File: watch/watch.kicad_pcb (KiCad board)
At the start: 2 copper layers, 118 parts, among them IC1 MAX77659AENV+, IC2 MAX86141ENP+T, IC3 MAX32664GTGC+T, IC4 TXS0108ERGYR, J1 TYPE-C-31-M-12, J2 Conn_01x02_Socket, J3 Conn_ARM_JTAG_SWD_10, J4 505110-2291, Q1 BSS138, U1 nRF52840, U2 ICM-20602, Y1 FA-128_32.0000MF10Z-AJ5, Y2 CM7V-T1A-32.768kHz-6pF-20PPM-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

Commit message: RTC, board started
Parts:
- removed S5: EVP-ATAL1B000, EVP-ATAL1B000:EVPATAL1B000
- added H1: MountingHole, mounting:watch-housing, F.Cu at (42.0, 32.0)
- added H2: MountingHole, mounting:watch-housing, F.Cu at (76.0, 32.0)
- added H3: MountingHole, mounting:watch-housing, F.Cu at (42.0, 65.0)
- added H4: MountingHole, mounting:watch-housing, F.Cu at (76.0, 65.0)
- added IC6: MAX31341CETB+T, MAX31341CETB+T:SON50P300X300X80-11N, F.Cu at (50.2, 59.2)
- added J5: Conn_01x01_Pin, TestPoint:TestPoint_Pad_4.0x4.0mm, F.Cu at (51.5, 36.0)
- added J6: Conn_01x01_Pin, TestPoint:TestPoint_Pad_1.5x1.5mm, B.Cu at (46.6, 44.0)
- added J7: Conn_01x01_Pin, TestPoint:TestPoint_Pad_1.5x1.5mm, B.Cu at (46.6, 41.0)
- added Y3: CM7V-T1A-32.768kHz-6pF-20PPM-TA-QC, CM7V-T1A-32.768kHz-6pF-20PPM-TA-QC:CM7V32768TBQA020, F.Cu at (46.2, 59.2)
- D1, D2, D3, J4: moved to B.Cu
- J2: value Conn_01x02_Socket -> Conn_01x01_Pin; footprint Connector_PinHeader_2.54mm:PinHeader_1x02_P2.54mm_Vertical -> TestPoint:TestPoint_Pad_4.0x4.0mm
- J3: footprint Connector_PinHeader_2.54mm:PinHeader_2x05_P2.54mm_Vertical -> Connector:Tag-Connect_TC2050-IDC-FP_2x05_P1.27mm_Vertical; moved to B.Cu
- moved IC1 117.6 mm to (47.1, 47.5)
- moved J2 106.5 mm to (46.5, 36.0)
- moved J1 105.9 mm to (59.0, 32.0), turned to 180 degrees
- moved IC3 101.0 mm to (53.5, 52.8)
- moved U2 99.8 mm to (59.0, 52.5)
- moved S4 98.3 mm to (47.0, 31.0), turned to 180 degrees
- moved J3 96.7 mm to (55.5, 61.4), turned to 180 degrees
- moved J4 94.9 mm to (59.0, 40.8), turned to 180 degrees
- moved D2 93.4 mm to (55.0, 53.0)
- moved U1 89.4 mm to (69.5, 56.2)
- moved LED3 86.8 mm to (50.0, 52.0), turned to 90 degrees
- moved LED2 86.3 mm to (48.0, 52.0), turned to -90 degrees
- moved LED1 86.2 mm to (45.8, 52.0), turned to -90 degrees
- moved IC4 81.3 mm to (71.3, 46.9)
- moved D3 80.9 mm to (59.0, 53.0), turned to -90 degrees
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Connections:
- U1 pad B9: unconnected-(U1-AIN6/P0.30-PadB9) -> ~{PMIC EN}
- U1 pad P23: unconnected-(U1-P1.07-PadP23) -> RTC D1
- U1 pad R24: unconnected-(U1-P1.06-PadR24) -> RTC CLKIN
- U1 pad T23: unconnected-(U1-P1.05-PadT23) -> RTC CLKOUT
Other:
- board outline added: 38 x 37 mm
- copper layers 2 -> 4

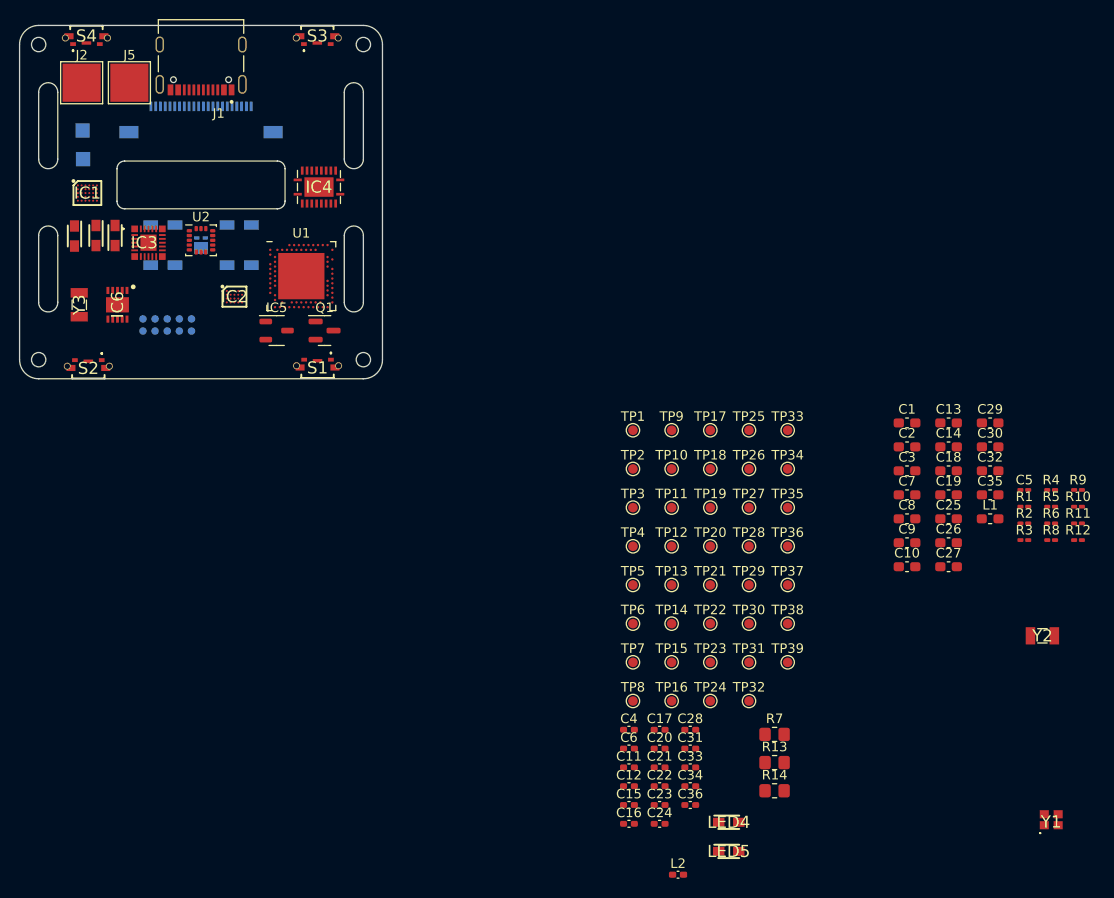
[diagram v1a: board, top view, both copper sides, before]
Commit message: rev1 done absolutely does not pass drc need to add ci
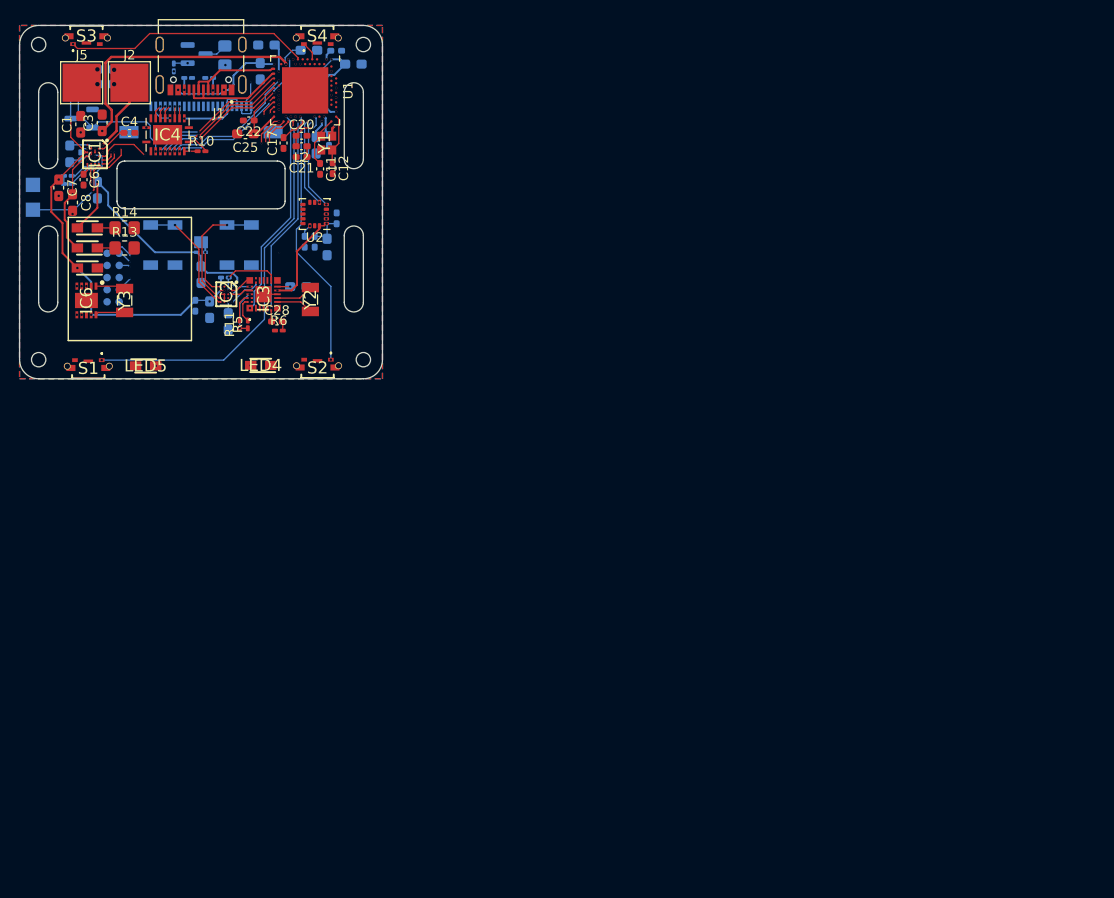
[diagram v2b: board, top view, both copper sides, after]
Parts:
- removed TP1, TP10, TP11, TP12, TP13, TP14, TP15, TP16, TP17, TP18, TP19, TP2, TP20, TP21, TP22, TP23, TP24, TP25, TP26, TP27, TP28, TP29, TP3, TP30, TP31, TP32, TP33, TP34, TP35, TP36, TP37, TP38, TP39, TP4, TP5, TP6, TP7, TP8, TP9: TestPoint, TestPoint:TestPoint_Pad_D1.0mm
- C10, C13, C14, C15, C16, C18, C19, C2, C23, C24, C26, C27, C29, C30, C31, C32, C33, C34, C35, C36, C5, C9, IC5, L1, Q1, R1, R12, R2, R3, R4, R7, R8, R9: moved to B.Cu
- moved R9 112.8 mm to (45.8, 37.5)
- moved R12 112.4 mm to (45.0, 45.8)
- moved R4 107.8 mm to (45.0, 46.6)
- moved C5 104.9 mm to (46.4, 43.7), turned to -90 degrees
- moved R8 104.4 mm to (56.1, 34.4), turned to 90 degrees
- moved Y1 103.8 mm to (72.2, 42.3), turned to -90 degrees
- moved L1 103.7 mm to (45.2, 43.5), turned to -90 degrees
- moved R2 99.2 mm to (57.6, 35.5), turned to 180 degrees
- moved R10 99.0 mm to (59.0, 43.2)
- moved C10 98.0 mm to (49.0, 36.1), turned to 180 degrees
- moved R1 96.4 mm to (59.9, 35.5)
- moved C7 94.5 mm to (44.1, 47.0), turned to -90 degrees
- moved C8 93.4 mm to (45.5, 48.5), turned to -90 degrees
- moved C2 92.8 mm to (49.0, 34.6), turned to 180 degrees
- moved C9 92.5 mm to (48.1, 47.2), turned to -90 degrees
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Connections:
- J4 pad 1: +3.3V -> VSSB1
- J4 pad 3: +3.3V -> VSSB1
- J4 pad 4: +3.3V -> VSSB1
- J4 pad 6: +3.3V -> VSSB1
- S2 pad 1: S3 -> S2
- S3 pad 1: S2 -> S3
- U1 pad A10: PMIC GPIO2 -> unconnected-(U1-AIN5/P0.29-PadA10)
- U1 pad AC11: TFTCS -> unconnected-(U1-P0.16-PadAC11)
- U1 pad AC17: ~{BIO RST} -> PMIC GPIO2
- U1 pad AC19: AX AD0 -> PMIC GPIO1
- U1 pad AD10: TFTDC -> TFTCS
- U1 pad AD12: TFTTE -> TFTMOSI
- U1 pad AD16: BIO MFIO -> TFTDC
- U1 pad AD18: AX IRQ -> ~{PMIC EN}
- U1 pad AD8: TFTMOSI -> TFTTE
- U1 pad B11: PMIC GPIO1 -> unconnected-(U1-AIN4/P0.28-PadB11)
- U1 pad B9: ~{PMIC EN} -> unconnected-(U1-AIN6/P0.30-PadB9)
- U1 pad G1: ~{TFTRST} 1V8 -> unconnected-(U1-P0.26-PadG1)
- U1 pad J1: unconnected-(U1-AIN2/P0.04-PadJ1) -> S4
- U1 pad J24: unconnected-(U1-NFC2/P0.10-PadJ24) -> AX AD0
- U1 pad L24: unconnected-(U1-NFC1/P0.09-PadL24) -> AX IRQ
- U1 pad P2: unconnected-(U1-P1.08-PadP2) -> ~{TFTRST} 1V8
- U1 pad P23: RTC D1 -> S2
- U1 pad R1: unconnected-(U1-TRACEDATA3/P1.09-PadR1) -> S3
- U1 pad R24: RTC CLKIN -> ~{BIO RST}
- U1 pad T23: RTC CLKOUT -> RTC D1
- U1 pad U24: S4 -> S1
- U1 pad V23: S3 -> RTC CLKIN
- U1 pad W24: S2 -> RTC CLKOUT
- U1 pad Y23: S1 -> BIO MFIO
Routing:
- net VSSB0: track 0.00 -> 95.2 mm, vias 0 -> 12
- net AX SCL: track 0.00 -> 68.2 mm, vias 0 -> 5
- net AX SDA: track 0.00 -> 67.8 mm, vias 0 -> 5
- net VDD_nRF: track 0.00 -> 60.5 mm, vias 0 -> 6
- net S1: track 0.00 -> 40.9 mm, vias 0 -> 2
- net JTAG RESET: track 0.00 -> 39.6 mm, vias 0 -> 2
- net RTC D1: track 0.00 -> 38.7 mm, vias 0 -> 2
- net VSSB1: track 0.00 -> 37.0 mm, vias 0 -> 3
- net RTC CLKOUT: track 0.00 -> 36.7 mm, vias 0 -> 2
- net RTC CLKIN: track 0.00 -> 36.7 mm, vias 0 -> 2
- net LED2: track 0.00 -> 36.3 mm, vias 0 -> 2
- net SWCLK: track 0.00 -> 35.6 mm, vias 0 -> 2
- net SWDIO: track 0.00 -> 34.2 mm, vias 0 -> 3
- net ~{TFTRST} 1V8: track 0.00 -> 34.1 mm, vias 0 -> 2
- net VDD: track 0.00 -> 33.8 mm, vias 0 -> 4
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- added copper zone on B.Cu, net -BATT
- added copper zone on F.Cu, net -BATT

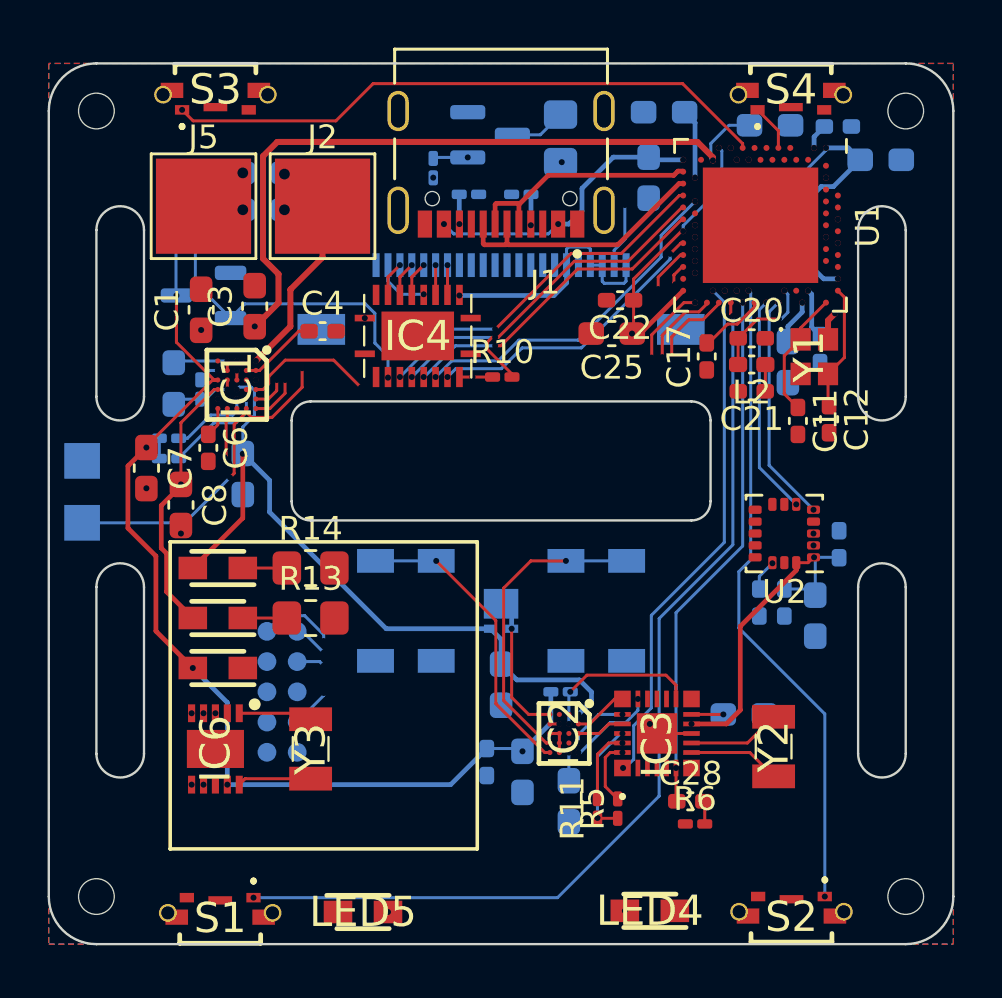
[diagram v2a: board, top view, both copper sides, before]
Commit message: rev0.1 done, passes drc and jlc checks
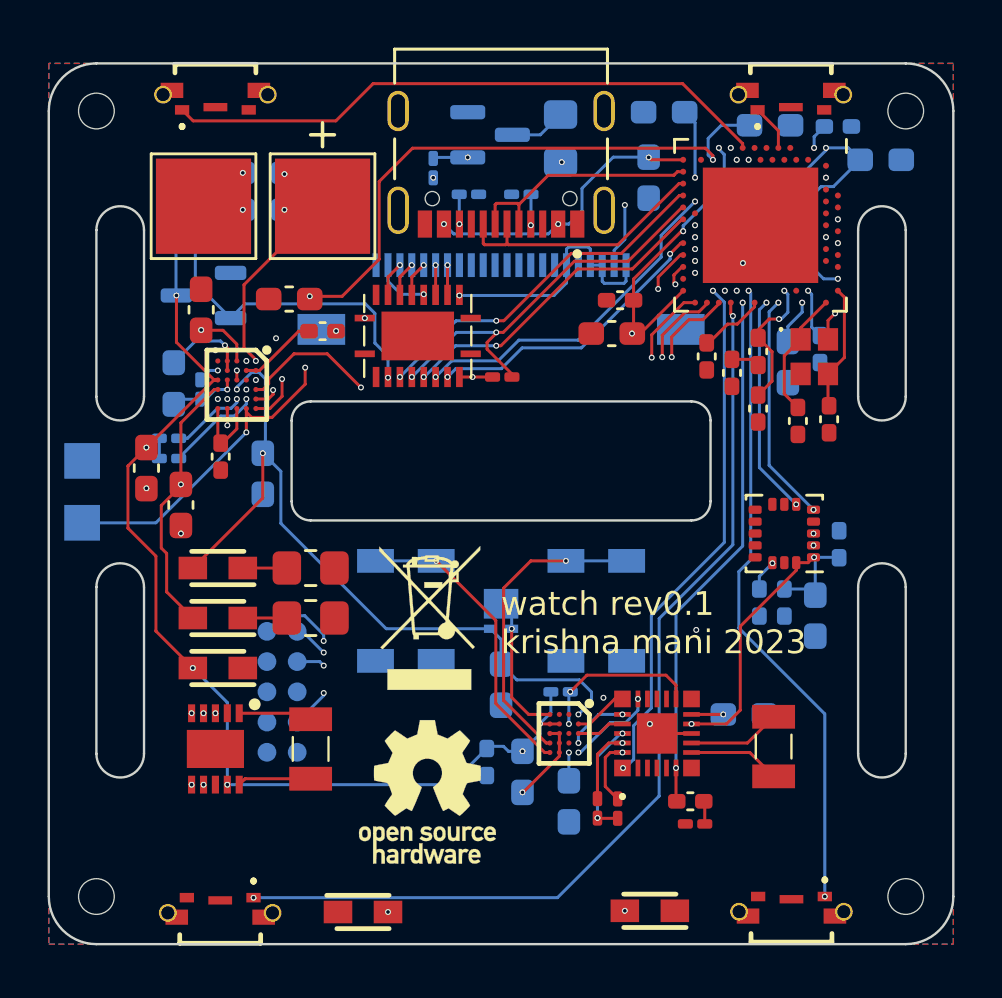
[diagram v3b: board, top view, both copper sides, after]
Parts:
- added G***: LOGO, custom:heart_highres, B.Cu at (55.0, 58.5)
- added G***: LOGO, custom:spo2_highres, B.Cu at (56.0, 62.0)
- added REF**: WEEE-Logo_4.2x6mm_SilkScreen, Symbol:WEEE-Logo_4.2x6mm_SilkScreen, F.Cu at (56.0, 53.3)
- added REF**: OSHW-Logo_5.7x6mm_SilkScreen, Symbol:OSHW-Logo_5.7x6mm_SilkScreen, F.Cu at (55.9, 60.6)
- moved C20 2.96 mm to (69.8, 44.5), turned to -90 degrees
- moved C3 1.48 mm to (50.1, 39.9), turned to 180 degrees
- moved C21 1.14 mm to (68.7, 43.0), turned to -90 degrees
- moved C9 0.84 mm to (49.0, 47.2)
- moved C6 0.64 mm to (47.2, 46.5)
- moved L2 0.61 mm to (69.8, 42.1), turned to 90 degrees
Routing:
- net -BATT: track 14.5 -> 19.6 mm, vias 10 -> 15
- net VDD: track 33.8 -> 29.6 mm
- net VIO: track 1.25 -> 3.28 mm
- net AX SDA: track 67.8 -> 66.3 mm
- net VSSB1: track 37.0 -> 38.2 mm
- net VSSB2: track 30.7 -> 31.9 mm
- net Net-(U1-ANT): track 4.61 -> 5.74 mm
- net Net-(IC1-LXA_1): track 2.68 -> 3.70 mm
- net ~{PMIC EN}: track 32.2 -> 31.4 mm
- net AX SCL: track 68.2 -> 68.8 mm
- net VBUS: track 27.1 -> 27.4 mm, vias 5 -> 4
- net SWDIO: vias 3 -> 2
- net S3: vias 1 -> 0
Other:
- board text added: "watch rev0.1 krishna mani 2023"

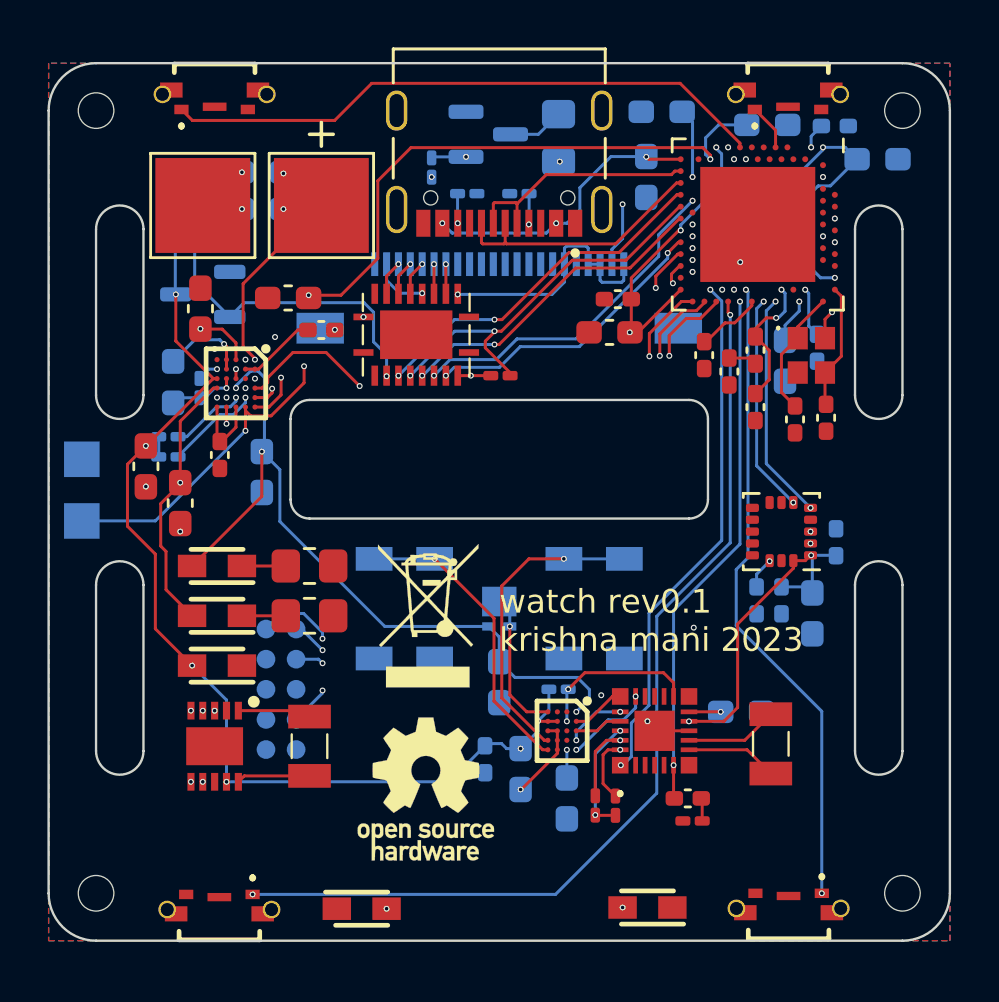
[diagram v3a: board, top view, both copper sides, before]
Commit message: change mounting clearances, add expansion connector
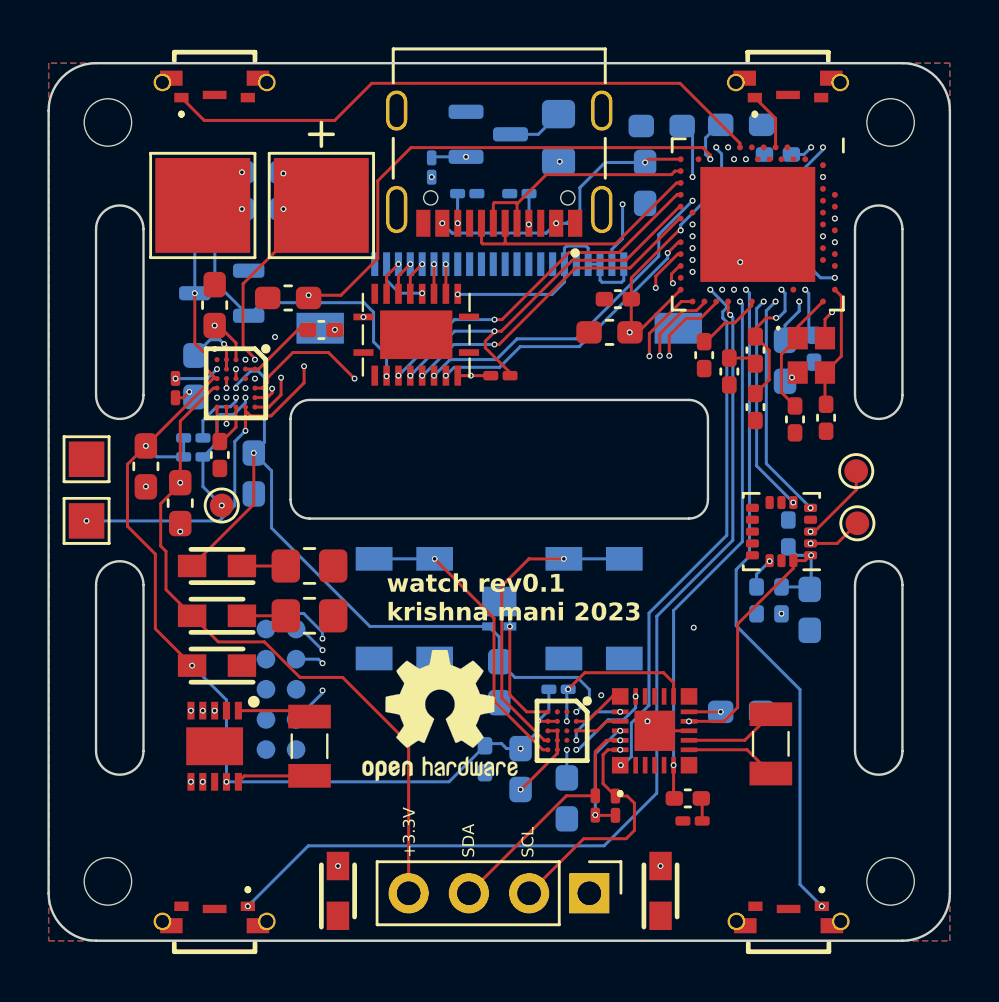
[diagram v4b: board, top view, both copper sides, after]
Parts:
- removed the REF** at (56.0, 53.3)
- removed the REF** at (55.9, 60.6)
- added J8: Conn_01x04_Pin, Connector_PinHeader_2.54mm:PinHeader_1x04_P2.54mm_Vertical, F.Cu at (62.8, 65.0)
- added REF**: OSHW-Logo2_7.3x6mm_SilkScreen, Symbol:OSHW-Logo2_7.3x6mm_SilkScreen, F.Cu at (56.5, 57.5)
- added TP1: TestPoint, TestPoint:TestPoint_Pad_D1.0mm, F.Cu at (74.0, 47.2)
- added TP15: TestPoint, TestPoint:TestPoint_Pad_D1.0mm, F.Cu at (47.3, 48.6)
- added TP2: TestPoint, TestPoint:TestPoint_Pad_D1.0mm, F.Cu at (74.1, 49.4)
- C5, J6, J7: moved to F.Cu
- moved C26 4.96 mm to (70.3, 35.9), turned to 180 degrees
- moved C15 2.68 mm to (70.8, 33.9), turned to 0 degrees
- moved C33 2.04 mm to (71.2, 49.8)
- moved LED5 1.25 mm to (52.2, 64.9), turned to 90 degrees
- moved C14 1.10 mm to (69.2, 32.6)
- moved R12 1.05 mm to (46.1, 45.8)
- moved R4 1.05 mm to (46.1, 46.6)
- moved C5 1.00 mm to (45.4, 43.7)
- moved L1 0.93 mm to (46.1, 43.2)
- moved LED4 0.89 mm to (65.8, 64.9), turned to 90 degrees
- moved R9 0.86 mm to (46.6, 37.4)
- moved IC5 0.80 mm to (47.3, 39.7)
- moved H1 0.71 mm to (42.5, 32.5)
- moved H2 0.71 mm to (75.5, 32.5)
- moved H3 0.71 mm to (42.5, 64.5)
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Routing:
- net VSSB1: track 38.2 -> 55.9 mm
- net AX SDA: track 66.3 -> 76.8 mm
- net AX SCL: track 68.8 -> 78.7 mm
- net VDD_nRF: track 60.4 -> 56.2 mm
- net LED1: track 32.0 -> 29.7 mm
- net ~{PMIC RST}: track 25.0 -> 26.9 mm, vias 2 -> 3
- net Net-(IC1-LXB_1): track 2.91 -> 1.09 mm, vias 1 -> 2
- net ~{PMIC EN}: track 31.4 -> 32.8 mm, vias 3 -> 4
- net LED2: track 36.3 -> 37.6 mm
- net VDD: track 29.6 -> 28.5 mm
- net VBUS: track 27.4 -> 26.3 mm
- net Net-(IC1-LXA_1): track 3.70 -> 2.70 mm
- net Net-(IC1-BST): track 0.91 -> 1.92 mm, vias 1 -> 2
- net ~{TFTRST} 1V8: track 34.1 -> 33.3 mm
- net ~{PMIC IRQ}: track 25.3 -> 24.6 mm
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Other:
- board text added: "+3.3V"
- board text added: "SCL"
- board text added: "SDA"
